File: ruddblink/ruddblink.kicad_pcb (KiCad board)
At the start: 2 copper layers, 40.6 x 48.5 mm, 31 parts, among them Q1 IRFML8244, SW1 JS202011JCQN, SW2 PTS526 SK15 SMTR2 LFS, U1 ATtiny85V-10SU, U2 74HC595

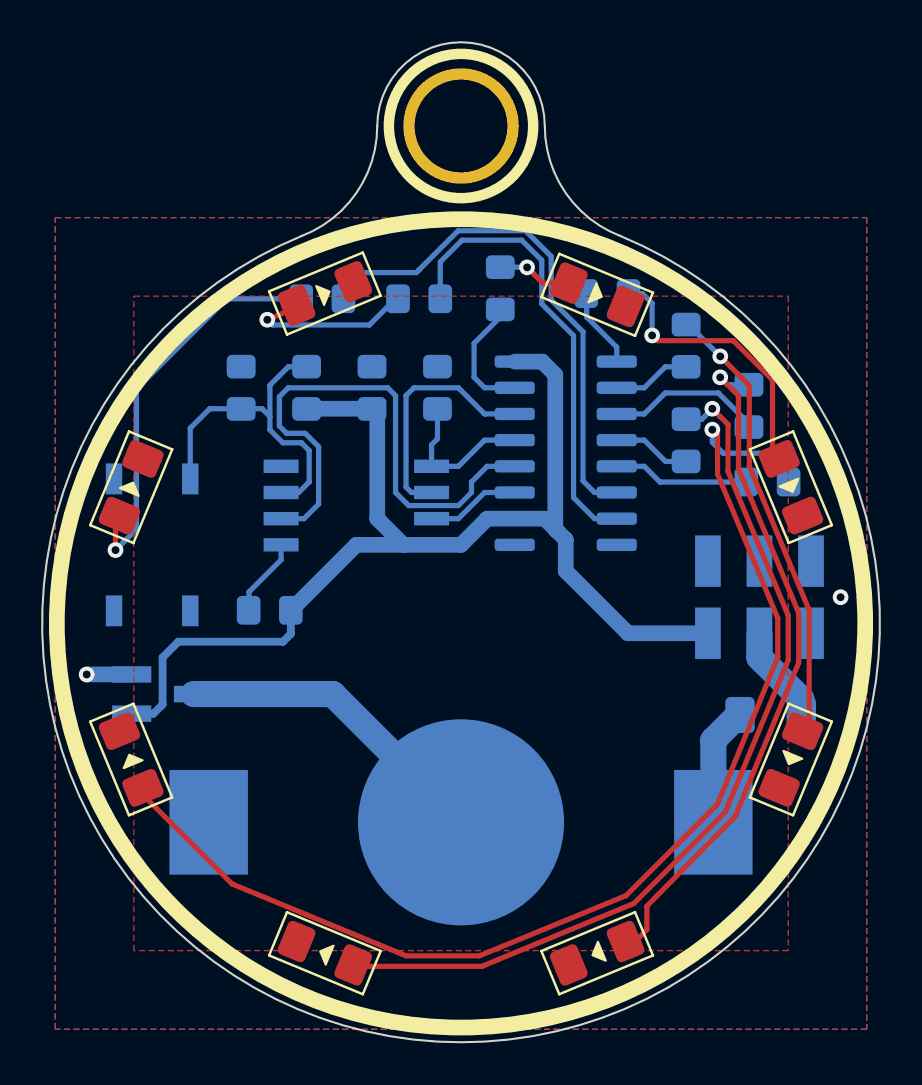
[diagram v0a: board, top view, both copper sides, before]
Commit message: replaced ruddock logo with usc solar car logo :)))
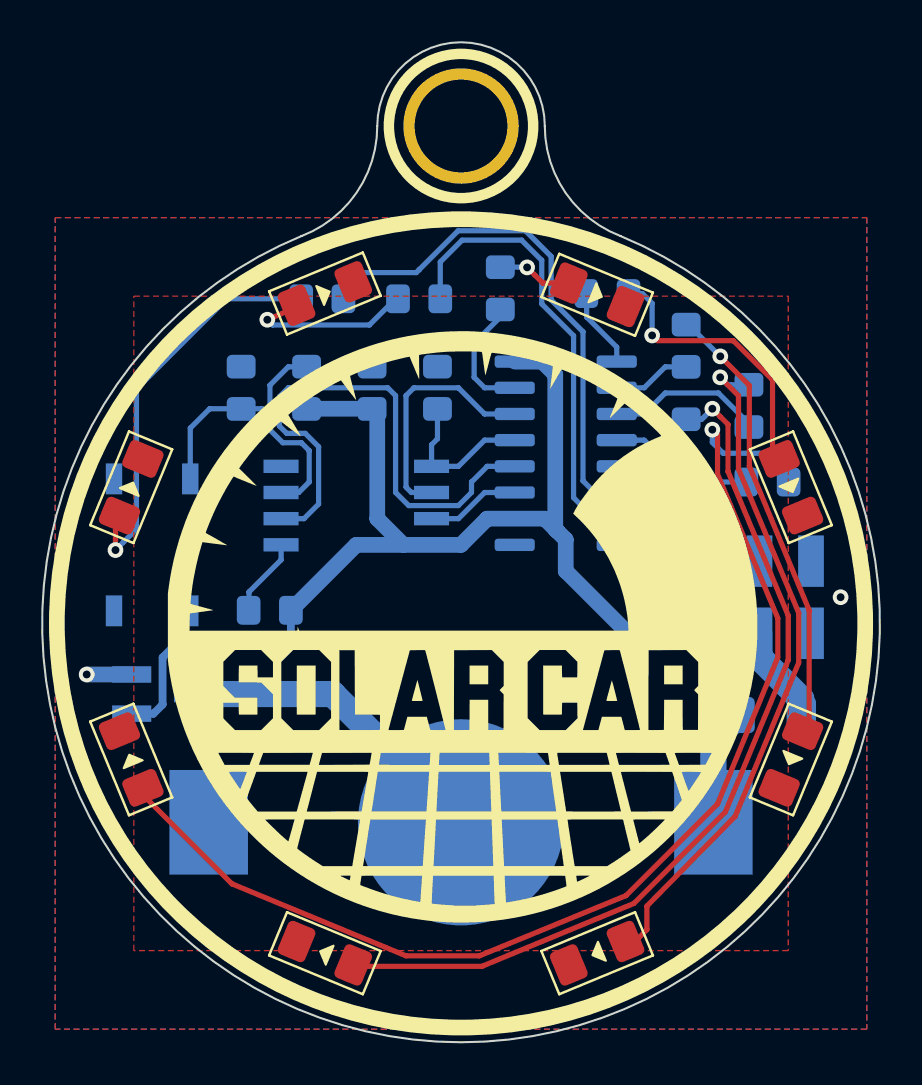
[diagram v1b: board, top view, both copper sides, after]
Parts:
- removed the G*** at (142.4, 114.6)
- added G***: , scsc_logo:sun+solar_mask_1in2, F.Cu at (142.4, 114.6)
- added G***: , scsc_logo:background_reduced_silk_1in2, F.Cu at (142.4, 114.6)
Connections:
- net /~OE renamed /~{OE}
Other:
- net class Default removed
- net class Power removed
- net class PowerThick removed
